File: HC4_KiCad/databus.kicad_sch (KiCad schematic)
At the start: 2 parts, among them IC8 74HC244, IC9 74HC244

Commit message: 進捗コミット2
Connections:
- net Immediate0 renamed Instruction_4
- net Immediate1 renamed Instruction_5
- net Immediate2 renamed Instruction_6
- net Immediate3 renamed Instruction_7

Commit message: I'm tired. あとは任せた　頑張りたまえ
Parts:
- added CP6, CP7: 0.1u, Capacitor_THT:C_Disc_D3.0mm_W1.6mm_P2.50mm, symbol Device2:C_Bypass
- added IC10: 74HC4002, symbol 74xx_2:74HC4002
- added J3: Expantion_Connector, Connector_PinHeader_2.54mm:PinHeader_2x20_P2.54mm_Vertical, symbol Connector_Generic:Conn_02x20_Odd_Even
- added LD2, LD3, LD4, LD5: LED, LED_THT:LED_Rectangular_W5.0mm_H2.0mm, symbol Device2:LED_
- added RN2: 1k, Resistor_THT:R_Array_SIP5, symbol Device:R_Network04_Split
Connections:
- net Databus0: now also IC10.2, J3.3 (Pin_3)
- net Databus1: now also IC10.3, J3.4 (Pin_4)
- net Databus2: now also IC10.4, J3.5 (Pin_5)
- net Databus3: now also IC10.5, J3.6 (Pin_6)
- net GND: now also CP6.2, CP7.2, J3.40 (Pin_40), RN2.1 (R1), RN2.1 (R1), RN2.1 (R1), RN2.1 (R1)
- net VCC: now also CP6.1, CP7.1, J3.39 (Pin_39)
- net at IC9.3 (2Y0): now also LD5.2
- net at IC9.5 (2Y1): now also LD4.2
- net at IC9.7 (2Y2): now also LD3.2
- net at IC9.9 (2Y3): now also LD2.2
- new net: LD4.1 (K), RN2.4 (R3.2)
- new net: LD3.1 (K), RN2.3 (R2.2)
- new net: LD5.1 (K), RN2.5 (R4.2)
- new net: LD2.1 (K), RN2.2 (R1.2)
- new net BUS_Zero: IC10.1
- new net CLK2: J3.28 (Pin_28)
- new net RAM_A0: J3.11 (Pin_11)
- new net RAM_A1: J3.12 (Pin_12)
- new net RAM_A2: J3.13 (Pin_13)
- new net RAM_A3: J3.14 (Pin_14)
- new net RAM_A4: J3.15 (Pin_15)
- new net RAM_A5: J3.16 (Pin_16)
- new net RAM_A6: J3.17 (Pin_17)
- new net RAM_A7: J3.18 (Pin_18)
- new net ~{RD}: J3.1 (Pin_1)
- new net ~{RESET}: J3.30 (Pin_30)
- new net ~{WR}: J3.2 (Pin_2)
- no-connect marks 0 -> 22
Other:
- title: (none) -> CPU

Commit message: 回路図の修正
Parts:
- removed IC8: 74HC244, symbol 74xx_2:74HC244
- added IC8: 74HC257, symbol 74xx_2:74HC257
- renumbered LD2 to LD4, LD3 to LD5, LD4 to LD6, LD5 to LD7
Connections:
- net ALU0: now also IC8.2 (I0a)
- net ALU1: now also IC8.5 (I0b)
- net ALU2: now also IC8.14 (I0c)
- net ALU3: now also IC8.11 (I0d)
- net Databus0: now also IC8.4 (Za)
- net Databus1: now also IC8.7 (Zb)
- net Databus2: now also IC8.12 (Zc)
- net Databus3: now also IC8.9 (Zd)
- net GND: now also IC8.8 (GND)
- net Level_C0: now also IC8.3 (I1a)
- net Level_C1: now also IC8.6 (I1b)
- net Level_C2: now also IC8.13 (I1c)
- net Level_C3: now also IC8.10 (I1d)
- net VCC: now also IC8.16 (VCC)
- net ~{ALU_OE}: now also IC8.15 (OE)
- net Instruction_4 renamed Instruction_0
- net Instruction_5 renamed Instruction_1
- net Instruction_6 renamed Instruction_2
- net Instruction_7 renamed Instruction_3
- new net Level_C_OE: IC8.1 (S)

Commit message: フットプリントの割り当て修正
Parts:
- IC10: footprint (none) -> Package_DIP:DIP-14_W7.62mm_Socket
- IC8: footprint (none) -> Package_DIP:DIP-16_W7.62mm_Socket
- IC9: footprint (none) -> Package_DIP:DIP-20_W7.62mm_Socket
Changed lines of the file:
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@@
 	(label "ALU0"
 		(at 81.28 57.15 0)
+		(fields_autoplaced yes)
 		(effects
 			(font
@@
 	(label "Databus1"
 		(at 121.92 123.19 180)
+		(fields_autoplaced yes)
 		(effects
 			(font
@@
 	(label "Stack0"
 		(at 137.16 106.68 0)
+		(fields_autoplaced yes)
 		(effects
 			(font
@@
 	(label "Databus1"
 		(at 76.2 133.35 0)
+		(fields_autoplaced yes)
 		(effects
 			(font
@@
 	(label "Level_C0"
 		(at 77.47 59.69 0)
+		(fields_autoplaced yes)
 		(effects
 			(font
@@
 	(label "Stack2"
 		(at 137.16 101.6 0)
+		(fields_autoplaced yes)
 		(effects
 			(font
@@
 	(label "Databus3"
 		(at 127 99.06 0)
+		(fields_autoplaced yes)
 		(effects
 			(font
@@
 	(label "Databus3"
 		(at 127 68.58 0)
+		(fields_autoplaced yes)
 		(effects
 			(font
@@
 	(label "Databus1"
 		(at 127 63.5 0)
+		(fields_autoplaced yes)
 		(effects
 			(font
@@
 	(label "Databus0"
 		(at 76.2 130.81 0)
+		(fields_autoplaced yes)
 		(effects
 			(font
@@
 	(label "Databus2"
 		(at 121.92 72.39 180)
+		(fields_autoplaced yes)
 		(effects
 			(font
@@
 	(label "Databus3"
 		(at 121.92 128.27 180)
+		(fields_autoplaced yes)
 		(effects
 			(font
@@
 	(label "Databus3"
 		(at 76.2 138.43 0)
+		(fields_autoplaced yes)
 		(effects
 			(font
@@
 	(label "Stack1"
 		(at 137.16 104.14 0)
+		(fields_autoplaced yes)
 		(effects
 			(font
@@
 	(label "Stack3"
 		(at 137.16 99.06 0)
+		(fields_autoplaced yes)
 		(effects
 			(font
@@
 	(label "Databus3"
 		(at 121.92 80.01 180)
+		(fields_autoplaced yes)
 		(effects
 			(font
@@
 	(label "Databus0"
 		(at 127 106.68 0)
+		(fields_autoplaced yes)
 		(effects
 			(font
@@
 	(label "Instruction_3"
 		(at 86.36 128.27 180)
+		(fields_autoplaced yes)
 		(effects
 			(font
@@
 	(label "RAM_A1"
 		(at 224.79 91.44 180)
+		(fields_autoplaced yes)
 		(effects
 			(font
@@
 	(label "RAM_A2"
 		(at 194.31 93.98 0)
+		(fields_autoplaced yes)
 		(effects
 			(font
@@
 	(label "ALU1"
 		(at 81.28 64.77 0)
+		(fields_autoplaced yes)
 		(effects
 			(font
@@
 	(label "RAM_A4"
 		(at 194.31 96.52 0)
+		(fields_autoplaced yes)
 		(effects
 			(font
@@
 	(label "Level_C2"
 		(at 77.47 74.93 0)
+		(fields_autoplaced yes)
 		(effects
 			(font
@@
 	(label "RAM_A5"
 		(at 224.79 96.52 180)
+		(fields_autoplaced yes)
 		(effects
 			(font
@@
 	(label "ALU2"
 		(at 81.28 72.39 0)
+		(fields_autoplaced yes)
 		(effects
 			(font
@@
 	(label "Databus1"
 		(at 121.92 64.77 180)
+		(fields_autoplaced yes)
 		(effects
 			(font
@@
 	(label "RAM_A6"
 		(at 194.31 99.06 0)
+		(fields_autoplaced yes)
 		(effects
 			(font
@@
 	(label "RAM_A7"
 		(at 224.79 99.06 180)
+		(fields_autoplaced yes)
 		(effects
 			(font
@@
 	(label "Level_C1"
 		(at 77.47 67.31 0)
+		(fields_autoplaced yes)
 		(effects
 			(font
@@
 	(label "Instruction_1"
 		(at 86.36 123.19 180)
+		(fields_autoplaced yes)
 		(effects
 			(font
@@
 	(label "Databus2"
 		(at 127 66.04 0)
+		(fields_autoplaced yes)
 		(effects
 			(font
@@
 	(label "Databus3"
 		(at 226.06 83.82 180)
+		(fields_autoplaced yes)
 		(effects
 			(font
@@
 	(label "Databus0"
 		(at 121.92 57.15 180)
+		(fields_autoplaced yes)
 		(effects
 			(font
@@
 	(label "RAM_A0"
 		(at 194.31 91.44 0)
+		(fields_autoplaced yes)
 		(effects
 			(font
@@
 	(label "Databus0"
 		(at 127 60.96 0)
+		(fields_autoplaced yes)
 		(effects
 			(font
@@
 	(label "Databus0"
 		(at 121.92 120.65 180)
+		(fields_autoplaced yes)
 		(effects
 			(font
@@
 	(label "Databus0"
 		(at 194.31 81.28 0)
+		(fields_autoplaced yes)
 		(effects
 			(font
@@
 	(label "Databus2"
 		(at 194.31 83.82 0)
+		(fields_autoplaced yes)
 		(effects
 			(font
@@
 	(label "Databus1"
 		(at 226.06 81.28 180)
+		(fields_autoplaced yes)
 		(effects
 			(font
@@
 	(label "Databus2"
 		(at 76.2 135.89 0)
+		(fields_autoplaced yes)
 		(effects
 			(font
@@
 	(label "Databus2"
 		(at 127 101.6 0)
+		(fields_autoplaced yes)
 		(effects
 			(font
@@
 	(label "Instruction_2"
 		(at 86.36 125.73 180)
+		(fields_autoplaced yes)
 		(effects
 			(font
@@
 	(label "Level_C3"
 		(at 77.47 82.55 0)
+		(fields_autoplaced yes)
 		(effects
 			(font
@@
 	(label "Instruction_0"
 		(at 86.36 120.65 180)
+		(fields_autoplaced yes)
 		(effects
 			(font
@@
 	(label "Databus2"
 		(at 121.92 125.73 180)
+		(fields_autoplaced yes)
 		(effects
 			(font
@@
 	(label "Databus1"
 		(at 127 104.14 0)
+		(fields_autoplaced yes)
 		(effects
 			(font
@@
 	(label "RAM_A3"
 		(at 224.79 93.98 180)
+		(fields_autoplaced yes)
 		(effects
 			(font
@@
 	(label "ALU3"
 		(at 81.28 80.01 0)
+		(fields_autoplaced yes)
 		(effects
 			(font
@@
 		(shape input)
 		(at 86.36 143.51 180)
+		(fields_autoplaced yes)
 		(effects
 			(font
@@
 		(shape output)
 		(at 147.32 99.06 0)
+		(fields_autoplaced yes)
 		(effects
 			(font
@@
 		(shape input)
 		(at 189.23 69.85 180)
+		(fields_autoplaced yes)
 		(effects
 			(font
@@
 		(shape input)
 		(at 86.36 87.63 180)
+		(fields_autoplaced yes)
 		(effects
 			(font
@@
 		(shape input)
 		(at 67.31 115.57 180)
+		(fields_autoplaced yes)
 		(effects
 			(font
@@
 		(shape input)
 		(at 72.39 57.15 180)
+		(fields_autoplaced yes)
 		(effects
 			(font
@@
 		(shape bidirectional)
 		(at 127 92.71 0)
+		(fields_autoplaced yes)
 		(effects
 			(font
@@
 		(shape input)
 		(at 215.9 78.74 0)
+		(fields_autoplaced yes)
 		(effects
 			(font
@@
 		(shape output)
 		(at 162.56 64.77 0)
+		(fields_autoplaced yes)
 		(effects
 			(font
@@
 		(shape input)
 		(at 86.36 90.17 180)
+		(fields_autoplaced yes)
 		(effects
 			(font
@@
 		(shape input)
 		(at 72.39 54.61 180)
+		(fields_autoplaced yes)
 		(effects
 			(font
@@
 		(shape input)
 		(at 203.2 78.74 180)
+		(fields_autoplaced yes)
 		(effects
 			(font
@@
 			)
 		)
-		(property "Footprint" ""
+		(property "Footprint" "Package_DIP:DIP-20_W7.62mm_Socket"
 			(at 99.06 133.35 0)
 			(effects
@@
 			)
 		)
-		(property "Footprint" ""
+		(property "Footprint" "Package_DIP:DIP-16_W7.62mm_Socket"
 			(at 99.06 72.39 0)
 			(effects
@@
 			)
 		)
-		(property "Footprint" ""
+		(property "Footprint" "Package_DIP:DIP-14_W7.62mm_Socket"
 			(at 144.78 64.77 0)
 			(effects

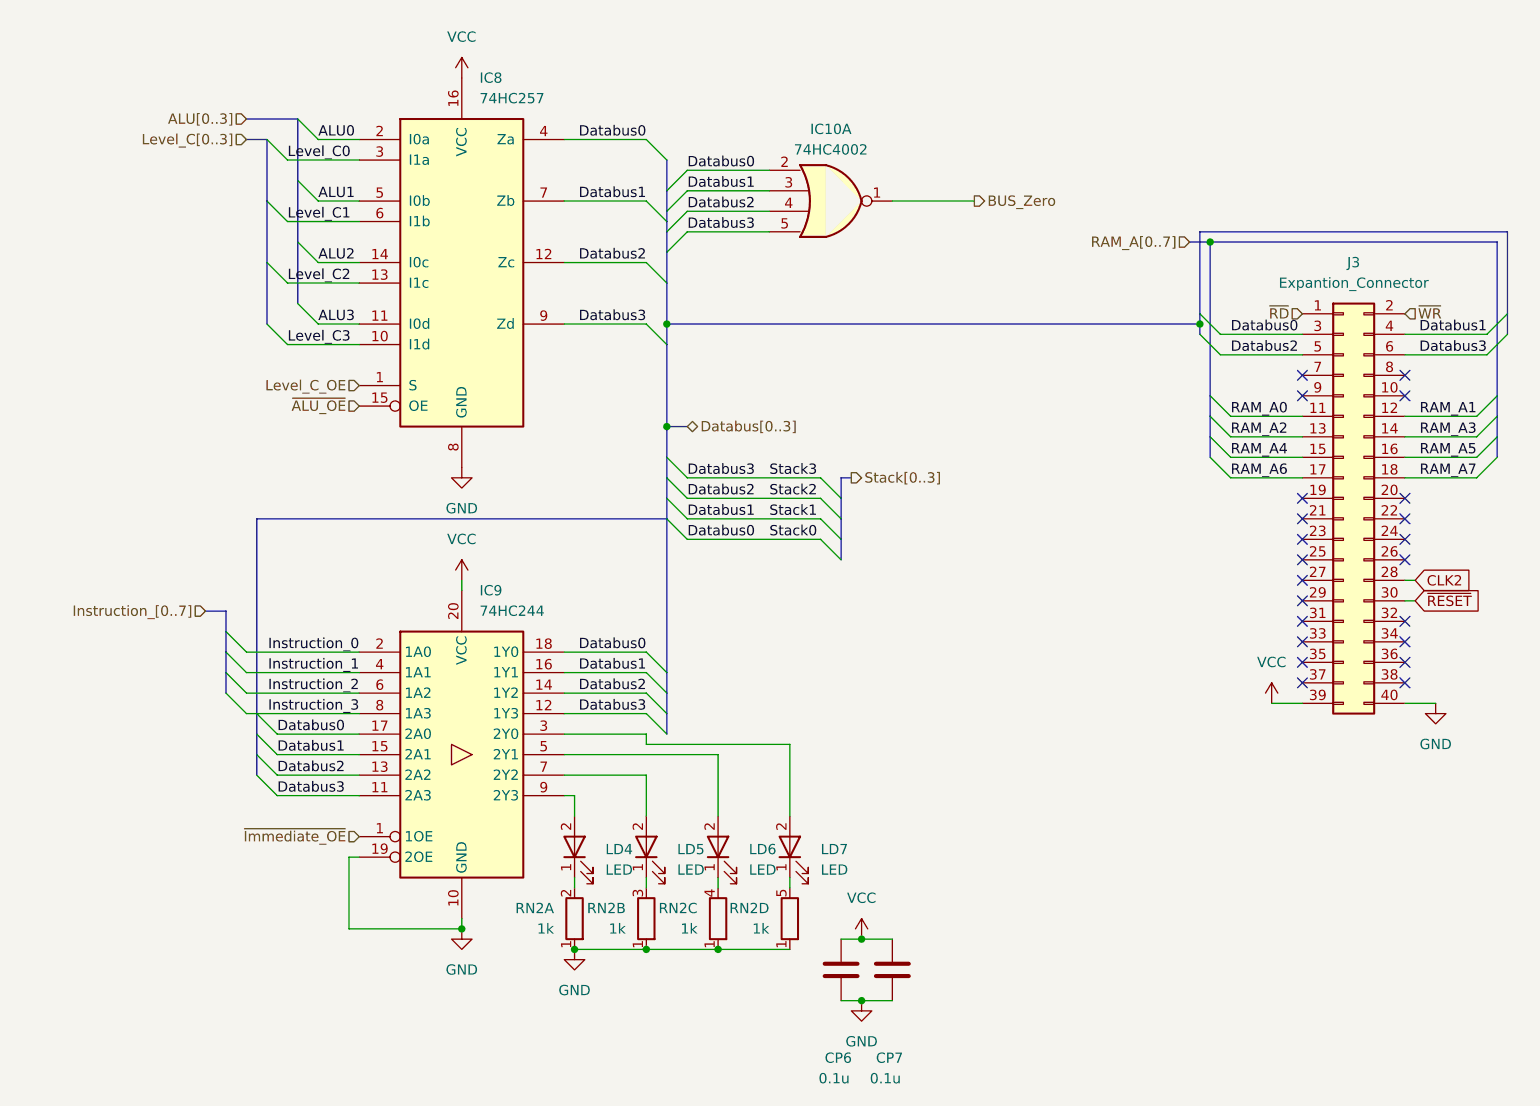
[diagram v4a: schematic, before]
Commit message: ICの配置を再検討
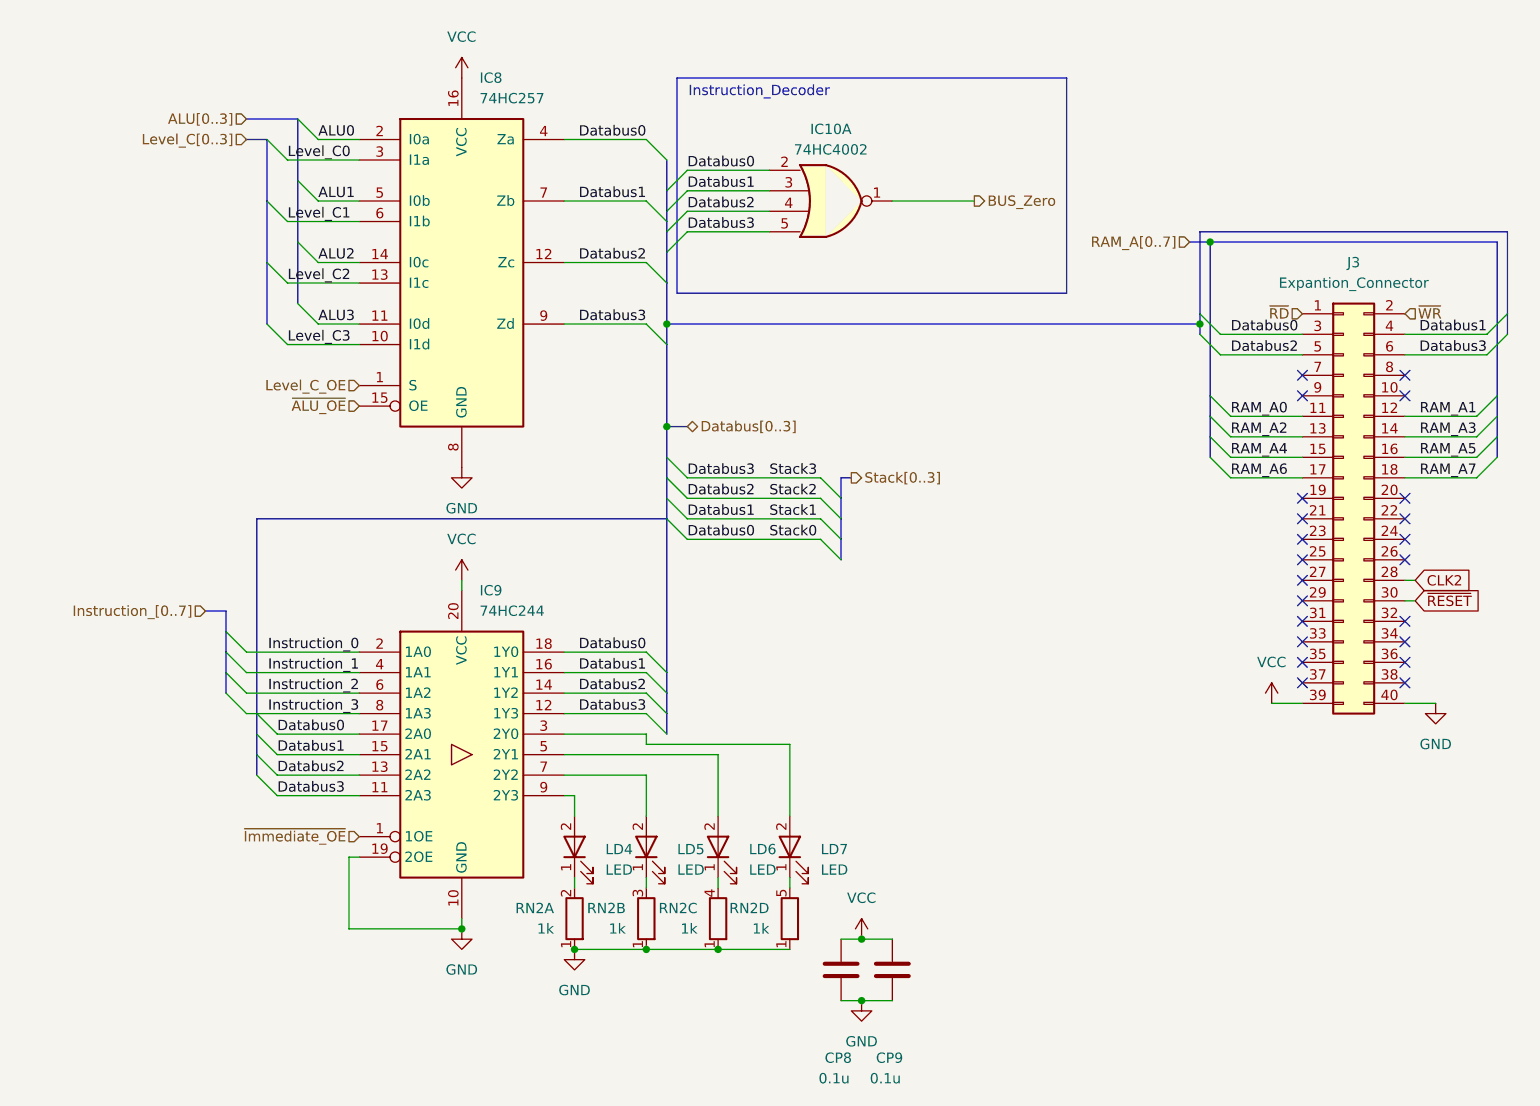
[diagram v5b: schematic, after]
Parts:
- renumbered CP6 to CP8, CP7 to CP9
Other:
- note added: "Instruction_Decoder"
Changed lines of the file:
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@@
+		)
+	)
+	(rectangle
+		(start 125.73 49.53)
+		(end 173.99 76.2)
+		(stroke
+			(width 0)
+			(type default)
+		)
+		(fill
+			(type none)
+		)
+	)
+	(text "Instruction_Decoder"
+		(exclude_from_sim no)
+		(at 135.89 51.308 0)
+		(effects
+			(font
+				(size 1.27 1.27)
+			)
 		)
 	)
 	(label "ALU0"
 		(at 81.28 57.15 0)
-		(fields_autoplaced yes)
 		(effects
 			(font
@@
 	(label "Databus1"
 		(at 121.92 123.19 180)
-		(fields_autoplaced yes)
 		(effects
 			(font
@@
 	(label "Stack0"
 		(at 137.16 106.68 0)
-		(fields_autoplaced yes)
 		(effects
 			(font
@@
 	(label "Databus1"
 		(at 76.2 133.35 0)
-		(fields_autoplaced yes)
 		(effects
 			(font
@@
 	(label "Level_C0"
 		(at 77.47 59.69 0)
-		(fields_autoplaced yes)
 		(effects
 			(font
@@
 	(label "Stack2"
 		(at 137.16 101.6 0)
-		(fields_autoplaced yes)
 		(effects
 			(font
@@
 	(label "Databus3"
 		(at 127 99.06 0)
-		(fields_autoplaced yes)
 		(effects
 			(font
@@
 	(label "Databus3"
 		(at 127 68.58 0)
-		(fields_autoplaced yes)
 		(effects
 			(font
@@
 	(label "Databus1"
 		(at 127 63.5 0)
-		(fields_autoplaced yes)
 		(effects
 			(font
@@
 	(label "Databus0"
 		(at 76.2 130.81 0)
-		(fields_autoplaced yes)
 		(effects
 			(font
@@
 	(label "Databus2"
 		(at 121.92 72.39 180)
-		(fields_autoplaced yes)
 		(effects
 			(font
@@
 	(label "Databus3"
 		(at 121.92 128.27 180)
-		(fields_autoplaced yes)
 		(effects
 			(font
@@
 	(label "Databus3"
 		(at 76.2 138.43 0)
-		(fields_autoplaced yes)
 		(effects
 			(font
@@
 	(label "Stack1"
 		(at 137.16 104.14 0)
-		(fields_autoplaced yes)
 		(effects
 			(font
@@
 	(label "Stack3"
 		(at 137.16 99.06 0)
-		(fields_autoplaced yes)
 		(effects
 			(font
@@
 	(label "Databus3"
 		(at 121.92 80.01 180)
-		(fields_autoplaced yes)
 		(effects
 			(font
@@
 	(label "Databus0"
 		(at 127 106.68 0)
-		(fields_autoplaced yes)
 		(effects
 			(font
@@
 	(label "Instruction_3"
 		(at 86.36 128.27 180)
-		(fields_autoplaced yes)
 		(effects
 			(font
@@
 	(label "RAM_A1"
 		(at 224.79 91.44 180)
-		(fields_autoplaced yes)
 		(effects
 			(font
@@
 	(label "RAM_A2"
 		(at 194.31 93.98 0)
-		(fields_autoplaced yes)
 		(effects
 			(font
@@
 	(label "ALU1"
 		(at 81.28 64.77 0)
-		(fields_autoplaced yes)
 		(effects
 			(font
@@
 	(label "RAM_A4"
 		(at 194.31 96.52 0)
-		(fields_autoplaced yes)
 		(effects
 			(font
@@
 	(label "Level_C2"
 		(at 77.47 74.93 0)
-		(fields_autoplaced yes)
 		(effects
 			(font
@@
 	(label "RAM_A5"
 		(at 224.79 96.52 180)
-		(fields_autoplaced yes)
 		(effects
 			(font
@@
 	(label "ALU2"
 		(at 81.28 72.39 0)
-		(fields_autoplaced yes)
 		(effects
 			(font
@@
 	(label "Databus1"
 		(at 121.92 64.77 180)
-		(fields_autoplaced yes)
 		(effects
 			(font
@@
 	(label "RAM_A6"
 		(at 194.31 99.06 0)
-		(fields_autoplaced yes)
 		(effects
 			(font
@@
 	(label "RAM_A7"
 		(at 224.79 99.06 180)
-		(fields_autoplaced yes)
 		(effects
 			(font
@@
 	(label "Level_C1"
 		(at 77.47 67.31 0)
-		(fields_autoplaced yes)
 		(effects
 			(font
@@
 	(label "Instruction_1"
 		(at 86.36 123.19 180)
-		(fields_autoplaced yes)
 		(effects
 			(font
@@
 	(label "Databus2"
 		(at 127 66.04 0)
-		(fields_autoplaced yes)
 		(effects
 			(font
@@
 	(label "Databus3"
 		(at 226.06 83.82 180)
-		(fields_autoplaced yes)
 		(effects
 			(font
@@
 	(label "Databus0"
 		(at 121.92 57.15 180)
-		(fields_autoplaced yes)
 		(effects
 			(font
@@
 	(label "RAM_A0"
 		(at 194.31 91.44 0)
-		(fields_autoplaced yes)
 		(effects
 			(font
@@
 	(label "Databus0"
 		(at 127 60.96 0)
-		(fields_autoplaced yes)
 		(effects
 			(font
@@
 	(label "Databus0"
 		(at 121.92 120.65 180)
-		(fields_autoplaced yes)
 		(effects
 			(font
@@
 	(label "Databus0"
 		(at 194.31 81.28 0)
-		(fields_autoplaced yes)
 		(effects
 			(font
@@
 	(label "Databus2"
 		(at 194.31 83.82 0)
-		(fields_autoplaced yes)
 		(effects
 			(font
@@
 	(label "Databus1"
 		(at 226.06 81.28 180)
-		(fields_autoplaced yes)
 		(effects
 			(font
@@
 	(label "Databus2"
 		(at 76.2 135.89 0)
-		(fields_autoplaced yes)
 		(effects
 			(font
@@
 	(label "Databus2"
 		(at 127 101.6 0)
-		(fields_autoplaced yes)
 		(effects
 			(font
@@
 	(label "Instruction_2"
 		(at 86.36 125.73 180)
-		(fields_autoplaced yes)
 		(effects
 			(font
@@
 	(label "Level_C3"
 		(at 77.47 82.55 0)
-		(fields_autoplaced yes)
 		(effects
 			(font
@@
 	(label "Instruction_0"
 		(at 86.36 120.65 180)
-		(fields_autoplaced yes)
 		(effects
 			(font
@@
 	(label "Databus2"
 		(at 121.92 125.73 180)
-		(fields_autoplaced yes)
 		(effects
 			(font
@@
 	(label "Databus1"
 		(at 127 104.14 0)
-		(fields_autoplaced yes)
 		(effects
 			(font
@@
 	(label "RAM_A3"
 		(at 224.79 93.98 180)
-		(fields_autoplaced yes)
 		(effects
 			(font
@@
 	(label "ALU3"
 		(at 81.28 80.01 0)
-		(fields_autoplaced yes)
 		(effects
 			(font
@@
 		(shape input)
 		(at 86.36 143.51 180)
-		(fields_autoplaced yes)
 		(effects
 			(font
@@
 		(shape output)
 		(at 147.32 99.06 0)
-		(fields_autoplaced yes)
 		(effects
 			(font
@@
 		(shape input)
 		(at 189.23 69.85 180)
-		(fields_autoplaced yes)
 		(effects
 			(font
@@
 		(shape input)
 		(at 86.36 87.63 180)
-		(fields_autoplaced yes)
 		(effects
 			(font
@@
 		(shape input)
 		(at 67.31 115.57 180)
-		(fields_autoplaced yes)
 		(effects
 			(font
@@
 		(shape input)
 		(at 72.39 57.15 180)
-		(fields_autoplaced yes)
 		(effects
 			(font
@@
 		(shape bidirectional)
 		(at 127 92.71 0)
-		(fields_autoplaced yes)
 		(effects
 			(font
@@
 		(shape input)
 		(at 215.9 78.74 0)
-		(fields_autoplaced yes)
 		(effects
 			(font
@@
 		(shape output)
 		(at 162.56 64.77 0)
-		(fields_autoplaced yes)
 		(effects
 			(font
@@
 		(shape input)
 		(at 86.36 90.17 180)
-		(fields_autoplaced yes)
 		(effects
 			(font
@@
 		(shape input)
 		(at 72.39 54.61 180)
-		(fields_autoplaced yes)
 		(effects
 			(font
@@
 		(shape input)
 		(at 203.2 78.74 180)
-		(fields_autoplaced yes)
 		(effects
 			(font
@@
 		(on_board yes)
 		(dnp no)
-		(property "Reference" "CP6"
+		(property "Reference" "CP8"
 			(at 144.018 170.942 0)
 			(effects
@@
 			(project "HC4_KiCad"
 				(path "/33731ded-38c0-4297-bdd8-92b082f46ff8/294cbb59-ed60-4be2-81ec-3da02c446083"
-					(reference "CP6")
+					(reference "CP8")
 					(unit 1)
 				)
@@
 		(on_board yes)
 		(dnp no)
-		(property "Reference" "CP7"
+		(property "Reference" "CP9"
 			(at 150.368 170.942 0)
 			(effects
@@
 			(project "HC4_KiCad"
 				(path "/33731ded-38c0-4297-bdd8-92b082f46ff8/294cbb59-ed60-4be2-81ec-3da02c446083"
-					(reference "CP7")
+					(reference "CP9")
 					(unit 1)
 				)
